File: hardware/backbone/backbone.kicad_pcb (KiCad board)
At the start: 4 copper layers, 31.3 x 68.9 mm, 83 parts, among them J1 RESET, J10 CORE_A, J11 MOUNT, J13 FIELD_B, J14 FIELD_A, J15 UART PROG, J2 FROM_PREVIOUS, J4 FROM_PREVIOUS, J5 CONN_A, J6 BOOTLOADER, J7 CONN_B, J8 CORE_B, J9 TO NEXT, Q2 AO3401A, U11 470nH DCR=450m, U13 470nH DCR=450m, U15 ST25R200, U17 BLM18PG471SZ1D, U2 SN65HVD230DR, U4 AP2112K-3.3TRG1, U5 ESP32-C3-MINI-1-H4X, U8 G3VM-61VY3, U9 SN74AHCT1G14DCKR, X1 NX2016SA 27.12MHz

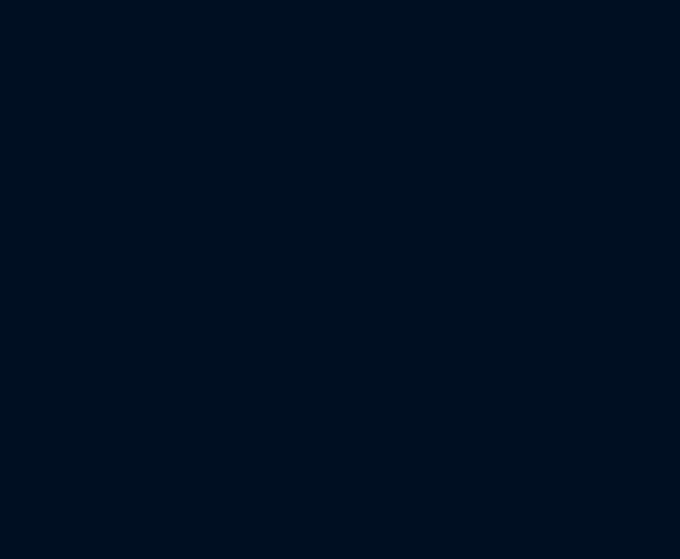
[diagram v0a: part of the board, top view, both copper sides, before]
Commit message: added hw libraries and pogo to backbone
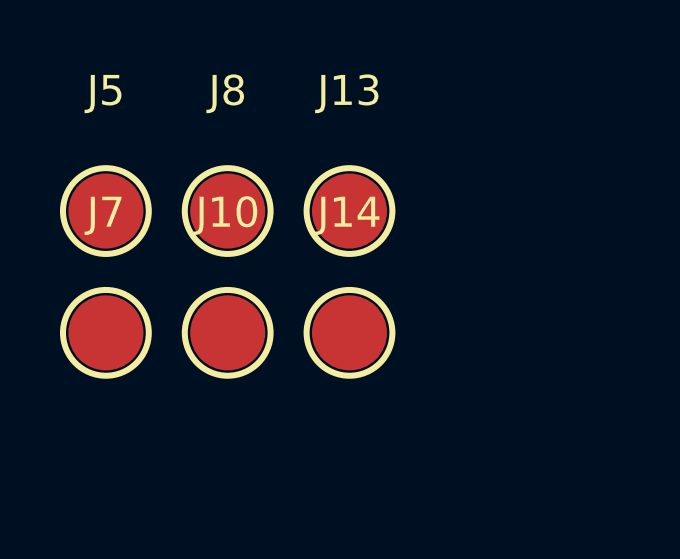
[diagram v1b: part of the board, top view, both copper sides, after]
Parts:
- added J10: CORE_A, SpaghettiLAB:SMD-1_BD2.0-H6.5, F.Cu at (5.59, 5.59)
- added J13: FIELD_B, SpaghettiLAB:SMD-1_BD2.0-H6.5, F.Cu at (9.65, 1.53)
- added J14: FIELD_A, SpaghettiLAB:SMD-1_BD2.0-H6.5, F.Cu at (9.65, 5.59)
- added J5: CONN_A, SpaghettiLAB:SMD-1_BD2.0-H6.5, F.Cu at (1.53, 1.53)
- added J7: CONN_B, SpaghettiLAB:SMD-1_BD2.0-H6.5, F.Cu at (1.53, 5.59)
- added J8: CORE_B, SpaghettiLAB:SMD-1_BD2.0-H6.5, F.Cu at (5.59, 1.53)
- U15: value ST25R200 -> ST25R100
